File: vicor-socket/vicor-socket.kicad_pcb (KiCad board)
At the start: 2 copper layers, 72.1 x 51.1 mm, 6 parts, among them J1 Interface, J2 HV+, J3 HV-, J4 12V+, J5 12V-, U1 DCM4623TD2J13D0T70-AEROParts

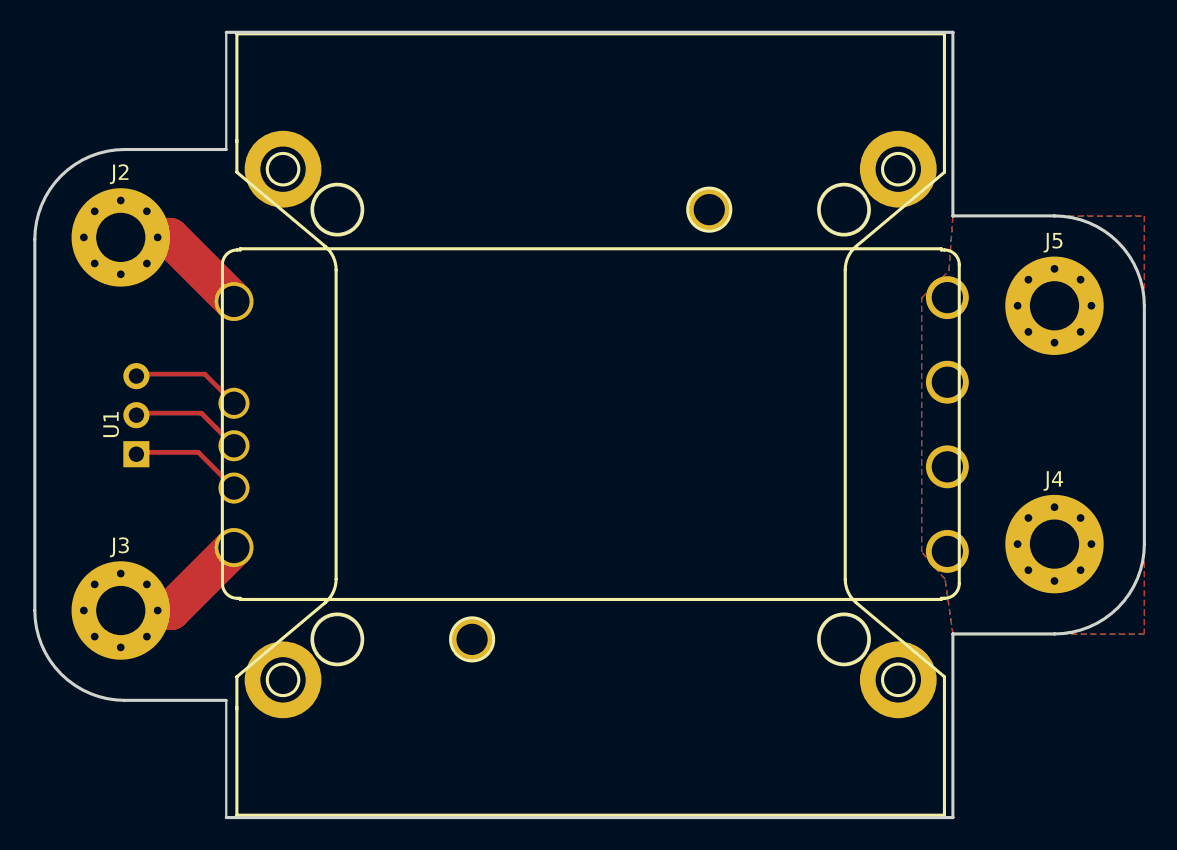
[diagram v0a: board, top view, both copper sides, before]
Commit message: Made lots of gerbers, shipped boards.
Also, re-routed interface-board to be 8/8mil minimum spacing.
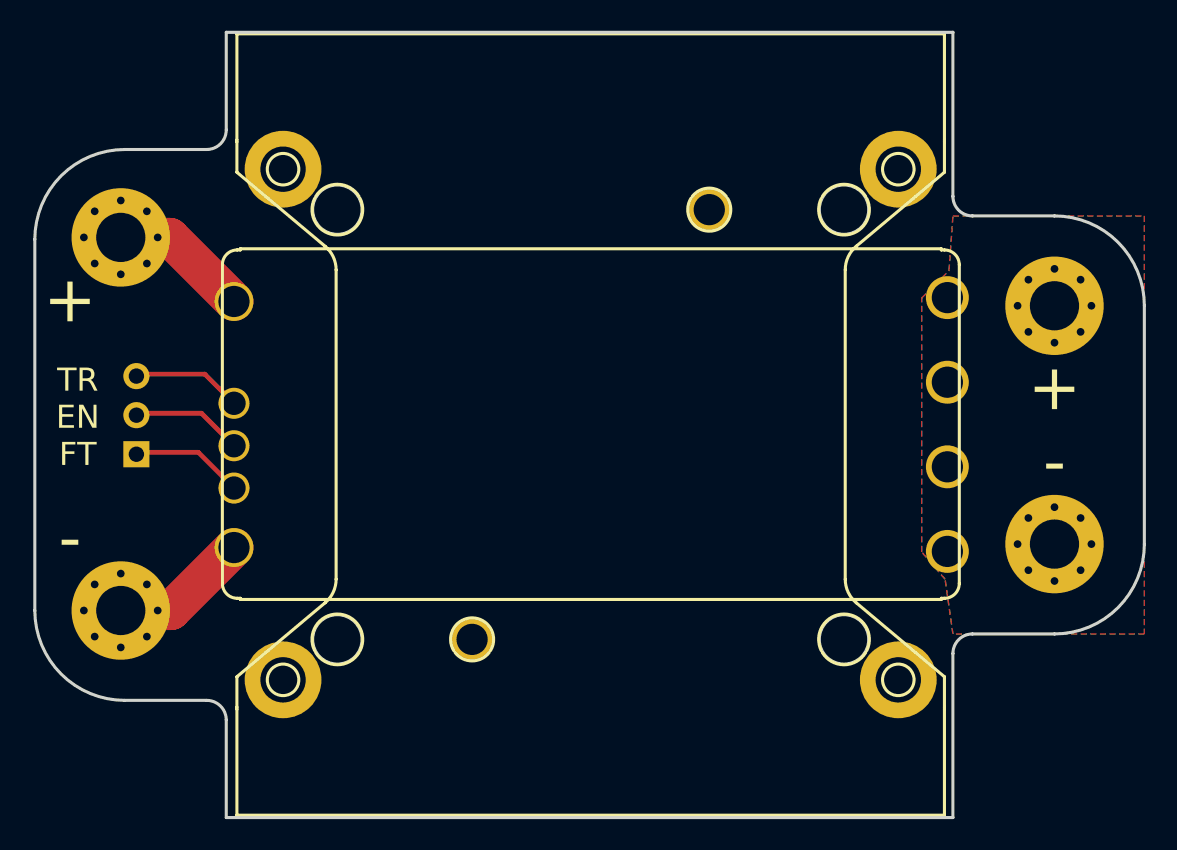
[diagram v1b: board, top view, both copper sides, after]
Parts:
- added G***: LOGO, AERO_Logos:AERO_Logo_30x12mm, B.Cu at (31.0, 11.4)
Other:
- outline, holes or cut-outs redrawn
- board text added: "+"
- board text added: "+ -"
- board text added: "-"
- board text added: "12V <-- 120-420V"
- board text added: "400W"
- board text added: "TR EN FT"
- board text added: "Vicor 4623 ChiP Carrier Board"
- board text added: "Willem Hillier 3/6/2019"

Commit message: Fully working interface-board firmware, fixed wrong polarity on vicor-socket
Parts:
- moved J4 15.5 mm to (60.7, 4.45)
- moved J5 15.5 mm to (60.7, 19.9)
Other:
- board text added: "This one has the correct polarity."
- board text added: "Willem Hillier 4/19/2019"
- board text removed: "Willem Hillier 3/6/2019"
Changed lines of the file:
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@@
   (general
     (thickness 1.6)
-    (drawings 34)
+    (drawings 35)
     (tracks 10)
     (zones 0)
@@
     (mod_text_size 1 1)
     (mod_text_width 0.15)
-    (pad_size 1.524 1.524)
-    (pad_drill 0.762)
+    (pad_size 6.4 6.4)
+    (pad_drill 3.2)
     (pad_to_mask_clearance 0.2)
     (solder_mask_min_width 0.25)
     (aux_axis_origin 0 0)
-    (grid_origin 55.372 -1.397)
+    (grid_origin 60.706 19.939)
     (visible_elements 7FFFFFFF)
     (pcbplotparams
@@
   )
   (module MountingHole:MountingHole_3.2mm_M3_Pad_Via (layer F.Cu)
-    (at 60.706 19.939)
+    (at 60.706 4.445)
     (descr "Mounting Hole 3.2mm, M3")
     (tags "mounting hole 3.2mm m3")
@@
   )
   (module MountingHole:MountingHole_3.2mm_M3_Pad_Via (layer F.Cu)
-    (at 60.706 4.445)
+    (at 60.706 19.939)
     (descr "Mounting Hole 3.2mm, M3")
     (tags "mounting hole 3.2mm m3")
@@
       (xy -0.036233 6.087603) (xy 2.502714 6.087603) (xy 1.784298 4.128375)) (layer B.SilkS) (width 0.01))
   )
+  (gr_text "This one has the\ncorrect polarity." (at 30.734 33.401) (layer B.SilkS)
+    (effects (font (size 1.5 1.5) (thickness 0.3)) (justify mirror))
+  )
   (dimension 51.308 (width 0.3) (layer F.SilkS)
     (gr_text "51.308 mm" (at 77.792 12.065 270) (layer F.SilkS)
@@
     (effects (font (size 1.5 1.5) (thickness 0.3)) (justify mirror))
   )
-  (gr_text "Willem Hillier  3/6/2019" (at 30.48 3.556) (layer B.SilkS)
+  (gr_text "Willem Hillier  4/19/2019" (at 30.48 3.556) (layer B.SilkS)
     (effects (font (size 1.5 1.5) (thickness 0.3)) (justify mirror))
   )
@@
       )
     )
+  )
+  (zone (net 0) (net_name "") (layer F.Mask) (hatch edge 0.508)
+    (connect_pads (clearance 0.508))
+    (min_thickness 0.254)
+    (fill yes (arc_segments 16) (thermal_gap 0.508) (thermal_bridge_width 0.508))
+    (polygon
+      (pts
+        (xy 53.594 21.971) (xy 56.896 21.971) (xy 56.896 18.923) (xy 53.594 18.923)
+      )
+    )
+  )
+  (zone (net 0) (net_name "") (layer F.Mask) (hatch edge 0.508)
+    (connect_pads (clearance 0.508))
+    (min_thickness 0.254)
+    (fill yes (arc_segments 16) (thermal_gap 0.508) (thermal_bridge_width 0.508))
+    (polygon
+      (pts
+        (xy 53.848 11.049) (xy 55.88 12.319) (xy 58.928 16.256) (xy 61.468 16.002) (xy 56.642 9.779)
+        (xy 54.356 8.001)
+      )
+    )
+  )
+  (zone (net 0) (net_name "") (layer B.Mask) (hatch edge 0.508)
+    (connect_pads (clearance 0.508))
+    (min_thickness 0.254)
+    (fill yes (arc_segments 16) (thermal_gap 0.508) (thermal_bridge_width 0.508))
+    (polygon
+      (pts
+        (xy 53.848 5.461) (xy 56.896 5.461) (xy 56.896 2.413) (xy 53.594 2.413)
+      )
+    )
+  )
+  (zone (net 0) (net_name "") (layer B.Mask) (hatch edge 0.508)
+    (connect_pads (clearance 0.508))
+    (min_thickness 0.254)
+    (fill yes (arc_segments 16) (thermal_gap 0.508) (thermal_bridge_width 0.508))
+    (polygon
+      (pts
+        (xy 54.356 16.383) (xy 59.436 13.081) (xy 62.23 8.255) (xy 58.928 8.001) (xy 56.642 11.557)
+        (xy 53.594 13.335)
+      )
+    )
